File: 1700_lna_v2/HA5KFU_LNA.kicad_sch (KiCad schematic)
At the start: 19 parts, among them J1 Conn_Coaxial, J2 Conn_Coaxial, J3 571-1-826629-2, U1 NCP163ASN330T1G, U2 QPL9547

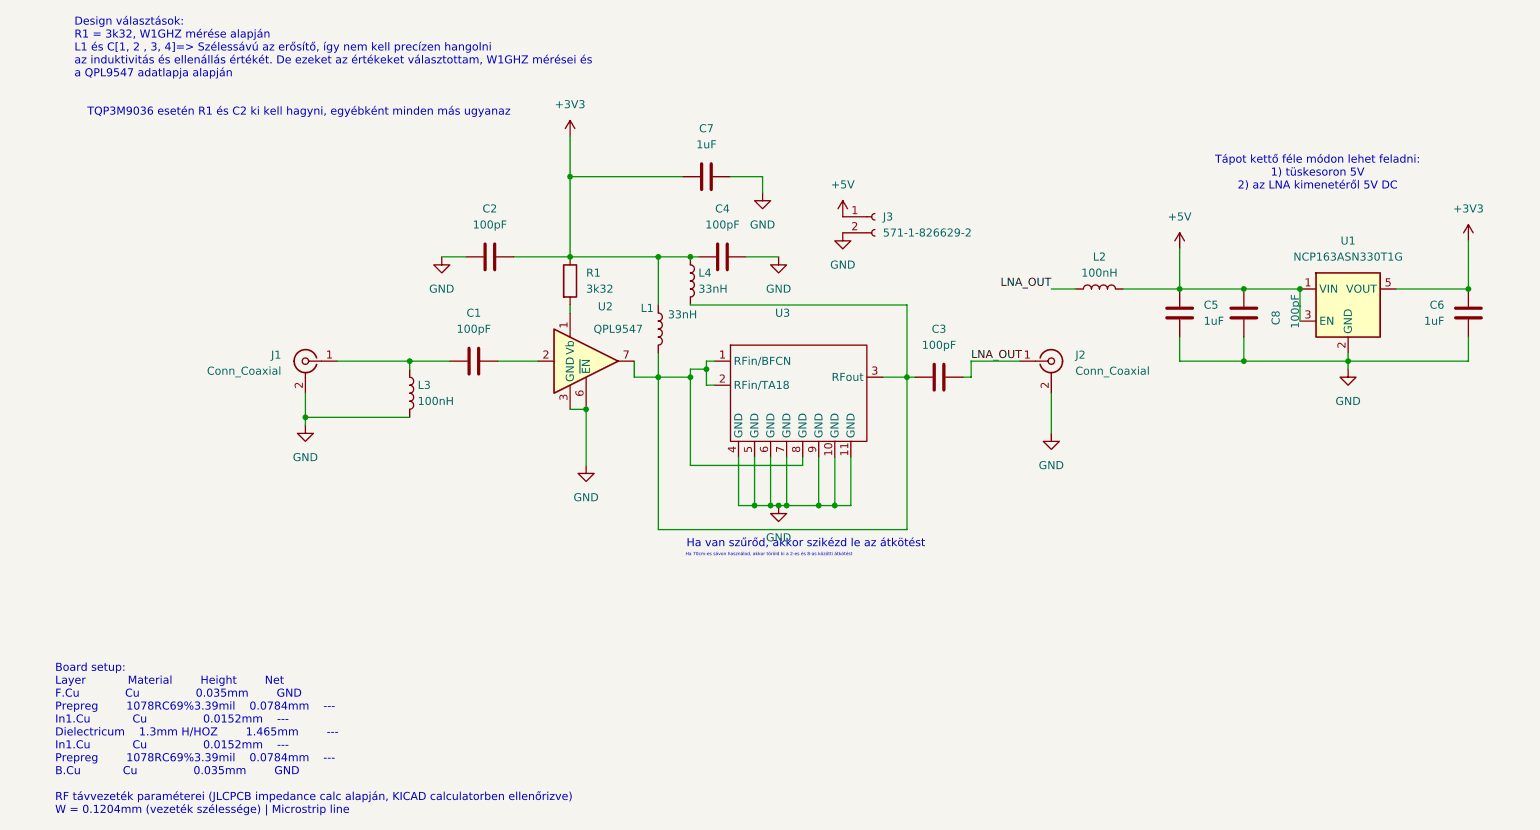
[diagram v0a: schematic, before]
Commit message: Added extra vias and power source selector
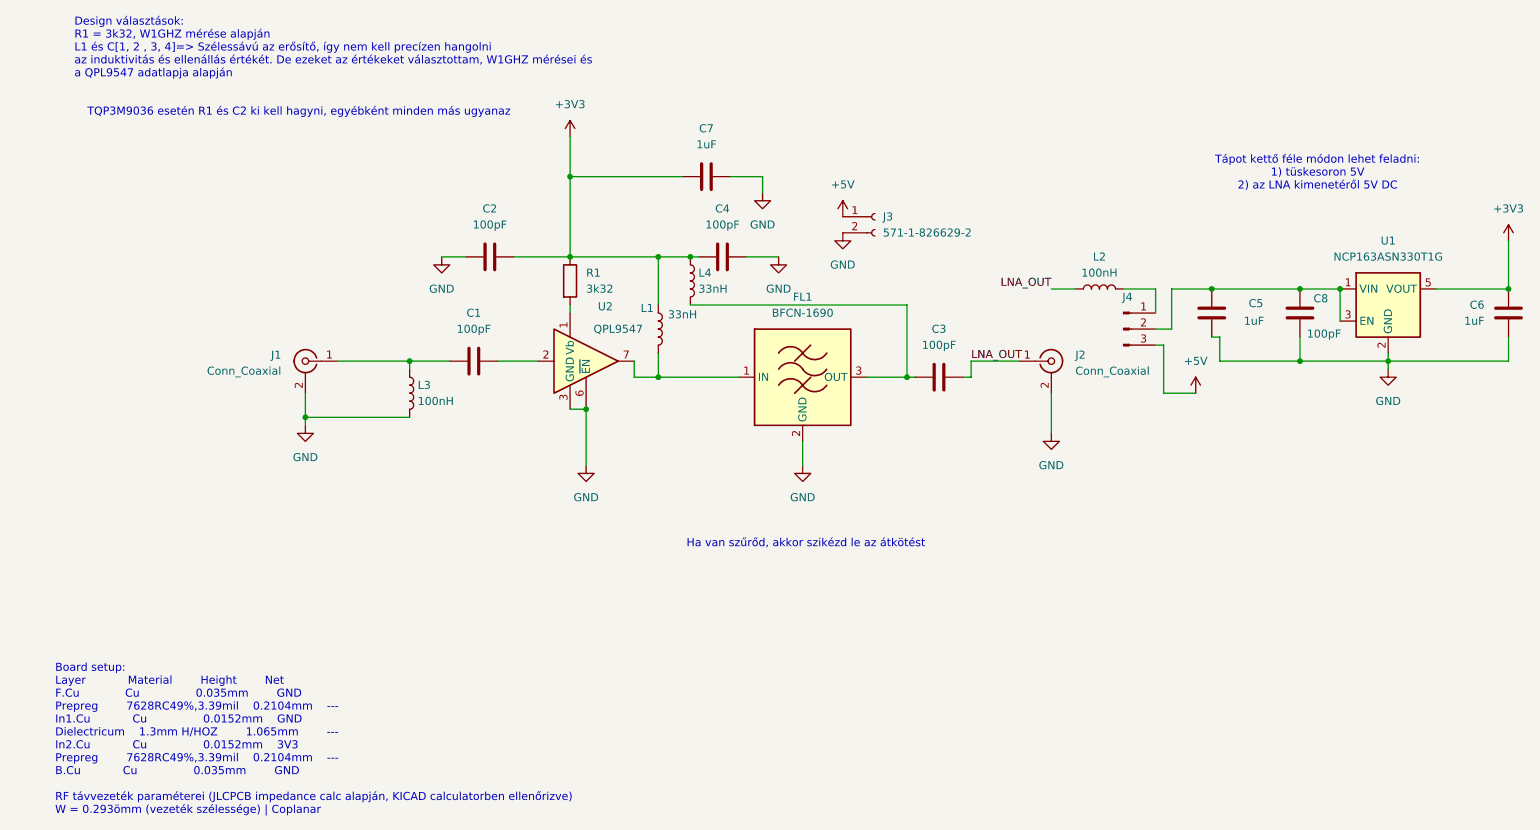
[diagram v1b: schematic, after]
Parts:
- removed U3: ~, SAW_filt2:Combined, symbol SAW_filt_sym:BFCN-TA1808
- added FL1: BFCN-1690, Filter:Filter_Mini-Circuits_FV1206-1, symbol RF_Filter:BFCN-1690
- added J4: Conn_01x03_Pin, Connector_PinHeader_2.54mm:PinHeader_1x03_P2.54mm_Vertical, symbol Connector:Conn_01x03_Pin
- J2: footprint Connector_Coaxial:SMA_Amphenol_132291_Vertical -> Connector_Coaxial:SMA_Amphenol_132134_Vertical
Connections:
- net +5V: now also J4.3 (Pin_3); no longer C5.1, C8.2, L2.2, U1.1 (VIN), U1.3 (EN)
- net GND: now also FL1.2 (GND), FL1.4 (GND), FL1.5 (GND), FL1.6 (GND)
- net at C3.1, L4.2: now also FL1.3 (OUT); no longer L1.2, U2.7
- new net: FL1.1 (IN), L1.2, U2.7
- new net: J4.1 (Pin_1), L2.2
- new net: C5.1, C8.2, J4.2 (Pin_2), U1.1 (VIN), U1.3 (EN)
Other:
- note added: "Board setup: Layer Material Height Net F.Cu Cu 0.035mm GND Prepreg 7628RC49%,3.39mil 0.2104mm --- In1.Cu Cu 0.0152mm GND Dielectricum 1.3mm H/HOZ 1.065mm --- In2.Cu Cu 0.0152mm 3V3 Prepreg 7628RC49%,3.39mil 0.2104mm --- B.Cu Cu 0.035mm GND RF távvezeték paraméterei (JLCPCB impedance calc alapján, KICAD calculatorben ellenőrizve) W = 0.293ömm (vezeték szélessége) | Coplanar"
- note removed: "Board setup: Layer Material Height Net F.Cu Cu 0.035mm GND Prepreg 1078RC69%3.39mil 0.0784mm --- In1.Cu Cu 0.0152mm --- Dielectricum 1.3mm H/HOZ 1.465mm --- In1.Cu Cu 0.0152mm --- Prepreg 1078RC69%3.39mil 0.0784mm --- B.Cu Cu 0.035mm GND RF távvezeték paraméterei (JLCPCB impedance calc alapján, KICAD calculatorben ellenőrizve) W = 0.1204mm (vezeték szélessége) | Microstrip line"
- note removed: "Ha 70cm-es sávon használod, akkor töröld ki a 2-es és 8-as közötti átkötést"
- moved on the sheet: C5, C6, C8, U1

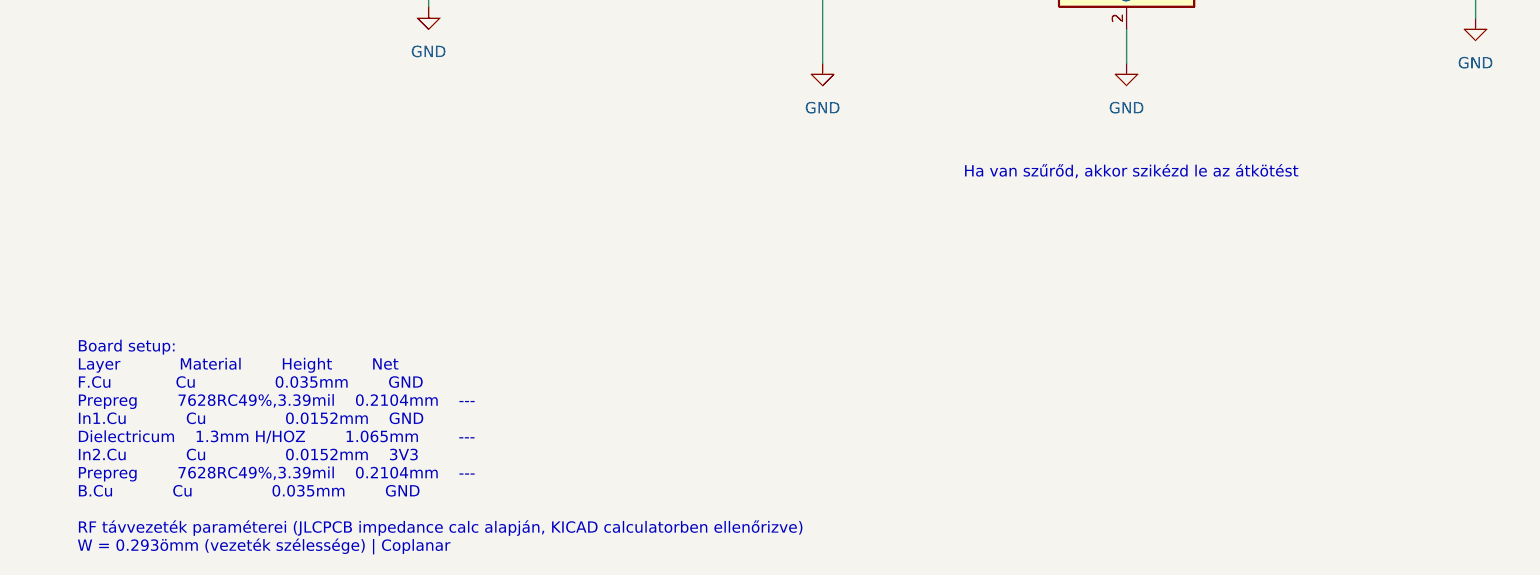
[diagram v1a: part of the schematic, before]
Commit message: Changed transmission line parameters
Changed transmission line width and ground plane to trace distance to better fit reduce parasitic capacitance.
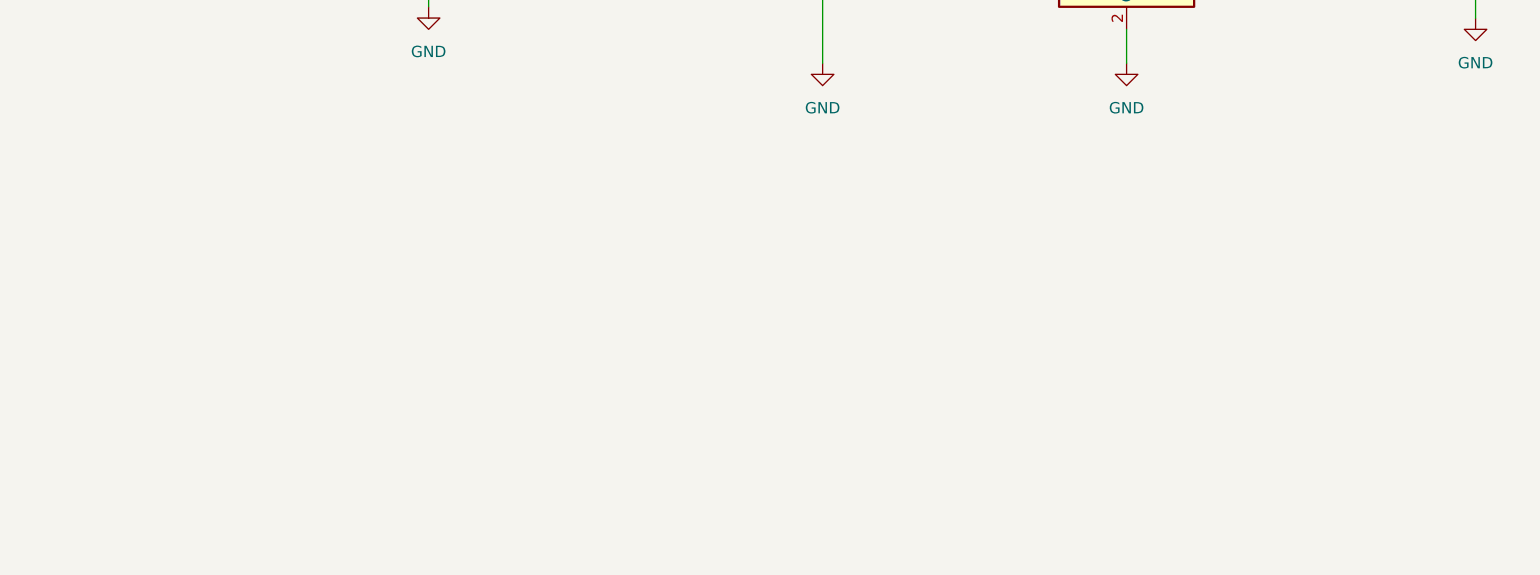
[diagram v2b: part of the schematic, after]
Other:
- note removed: "Board setup: Layer Material Height Net F.Cu Cu 0.035mm GND Prepreg 7628RC49%,3.39mil 0.2104mm --- In1.Cu Cu 0.0152mm GND Dielectricum 1.3mm H/HOZ 1.065mm --- In2.Cu Cu 0.0152mm 3V3 Prepreg 7628RC49%,3.39mil 0.2104mm --- B.Cu Cu 0.035mm GND RF távvezeték paraméterei (JLCPCB impedance calc alapján, KICAD calculatorben ellenőrizve) W = 0.293ömm (vezeték szélessége) | Coplanar"
- note removed: "Ha van szűrőd, akkor szikézd le az átkötést"
